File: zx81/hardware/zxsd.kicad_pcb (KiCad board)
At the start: 2 copper layers, 69.9 x 95.9 mm, 40 parts, among them J1 Micro_SD_Card, J2 ZX81_EXP, Q1 BC547, SW1 RESET, U1 74LS32, U10 27C256, U11 KM62256CLP, U2 74HC74, U3 74LS00, U4 74LS02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

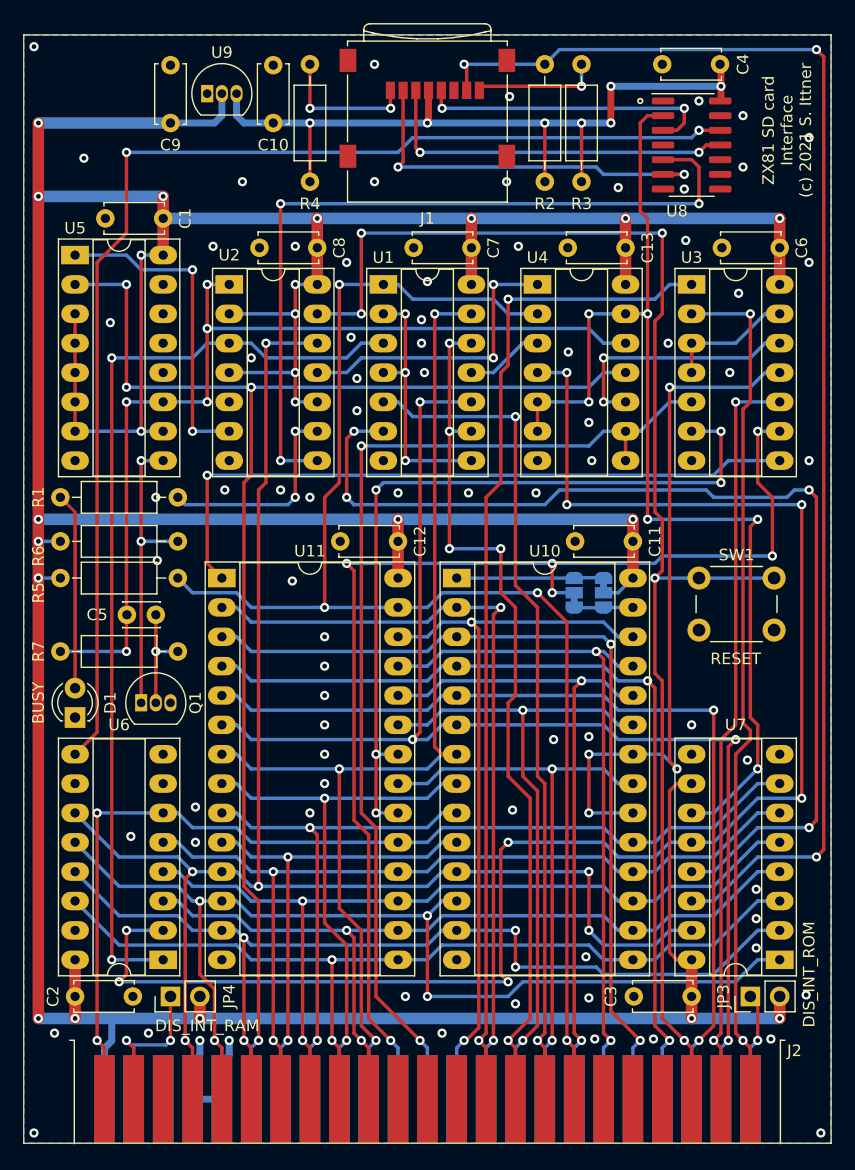
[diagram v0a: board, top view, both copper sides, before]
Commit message: fixed rom chip select
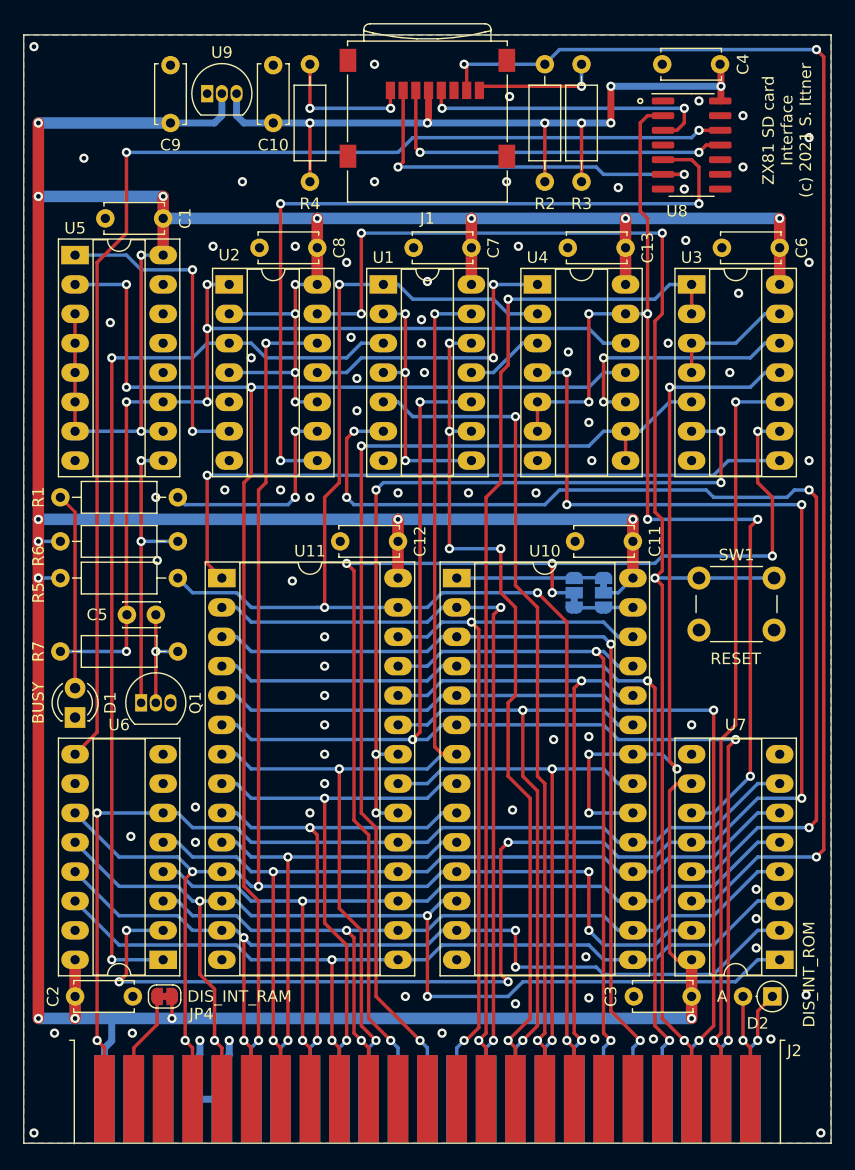
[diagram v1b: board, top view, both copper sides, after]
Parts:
- removed JP3: DIS_INT_ROM, Connector_PinHeader_2.54mm:PinHeader_1x02_P2.54mm_Vertical
- added D2: BAT43, Diode_THT:D_DO-35_SOD27_P2.54mm_Vertical_AnodeUp, F.Cu at (177.2, 126.4)
- C5: value 4p7 -> 470p
- JP4: footprint Connector_PinHeader_2.54mm:PinHeader_1x02_P2.54mm_Vertical -> Jumper:SolderJumper-2_P1.3mm_Bridged_RoundedPad1.0x1.5mm
- U1: value 74LS32 -> 74HCT32
- U2: value 74HC74 -> 74HCT74
- U3: value 74LS00 -> 74HCT00
- U4: value 74LS02 -> 74HCT02
- U5: value 74LS163 -> 74HCT163
- U6: value 74HC165 -> 74HCT165
- U7: value 74HC595 -> 74HCT595
- moved JP4 0.51 mm to (124.6, 126.4), turned to 180 degrees
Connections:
- JP4 pad 1: /nRAMCS_INT -> +5V
- JP4 pad 2: +5V -> /nRAMCS_INT
- U3 pad 2: /nRFSH -> /nMREQ
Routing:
- net /nRFSH: track 74.6 -> 9.15 mm, vias 2 -> 1
- net +5V: track 420.0 -> 410.5 mm, vias 23 -> 22
- net /nRAMCS_INT: track 13.3 -> 9.73 mm, vias 2 -> 0
- net /nMREQ: track 86.9 -> 89.5 mm
- net /SD_CLK: track 95.4 -> 94.9 mm
- net GND: vias 77 -> 76

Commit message: simplified sd card interface
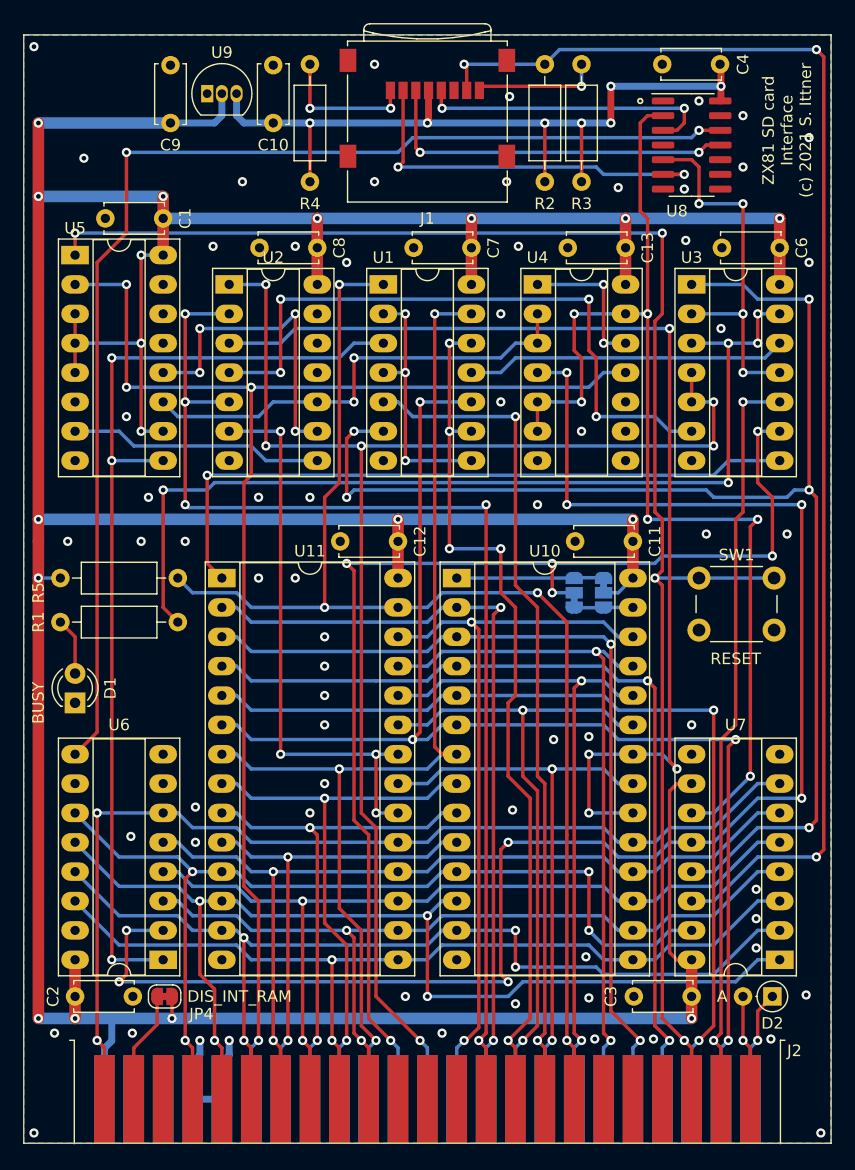
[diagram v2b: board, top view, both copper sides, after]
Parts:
- removed C5: 470p, Capacitor_THT:C_Disc_D3.0mm_W2.0mm_P2.50mm
- removed Q1: BC547, Package_TO_SOT_THT:TO-92_Inline
- removed R6: 1k, Resistor_THT:R_Axial_DIN0207_L6.3mm_D2.5mm_P10.16mm_Horizontal
- removed R7: 47k, Resistor_THT:R_Axial_DIN0207_L6.3mm_D2.5mm_P10.16mm_Horizontal
- U2: value 74HCT74 -> 74HCT32
- moved R1 10.8 mm to (115.6, 94.0)
- moved D1 1.27 mm to (116.8, 101.0)
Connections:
- U2 pad 1: Net-(C5-Pad2) -> /A14
- U2 pad 10: +5V -> Net-(U2-Pad10)
- U2 pad 11: Net-(U2-Pad11) -> (no net)
- U2 pad 12: /D0 -> GND
- U2 pad 13: /nRESET -> GND
- U2 pad 2: +5V -> /nMREQ
- U2 pad 3: /nSDWR -> /nCS_ROM
- U2 pad 4: +5V -> Net-(U2-Pad4)
- U2 pad 5: (no net) -> /nMREQ
- U2 pad 6: Net-(U2-Pad6) -> /nCS_RAM
- U2 pad 8: /nSD_SEL -> Net-(U2-Pad8)
- U2 pad 9: Net-(R1-Pad2) -> Net-(U2-Pad9)
- U3 pad 1: /nMREQ -> /nSDRD
- U3 pad 11: /nCS_ROM -> /nSD_SEL
- U3 pad 12: Net-(U3-Pad12) -> Net-(U1-Pad11)
- U3 pad 13: Net-(U3-Pad13) -> Net-(R1-Pad2)
- U3 pad 2: /nMREQ -> /nSD_SEL
- U3 pad 3: Net-(U3-Pad13) -> Net-(R1-Pad2)
- U3 pad 4: Net-(U3-Pad13) -> /A14
- U3 pad 6: /nCS_RAM -> Net-(U2-Pad4)
- U4 pad 1: Net-(U2-Pad11) -> Net-(U4-Pad1)
- U4 pad 10: Net-(U3-Pad12) -> (no net)
- U4 pad 12: Net-(C5-Pad2) -> Net-(U4-Pad1)
- U4 pad 2: /nWR -> Net-(U2-Pad10)
- U4 pad 3: Net-(U1-Pad11) -> Net-(U2-Pad10)
- U4 pad 8: /A14 -> GND
- U4 pad 9: /A14 -> GND
- U5 pad 1: Net-(U2-Pad6) -> /nRESET
- U5 pad 11: Net-(C5-Pad2) -> Net-(U2-Pad10)
- U5 pad 12: (no net) -> Net-(U2-Pad9)
- U5 pad 6: +5V -> GND
- U5 pad 7: +5V -> Net-(U2-Pad8)
- U5 pad 9: Net-(Q1-Pad1) -> /nSDWR
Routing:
- net Net-(C5-Pad2): track 83.1 -> 0.00 mm, vias 5 -> 0
- net Net-(R1-Pad2): track 18.3 -> 83.3 mm, vias 2 -> 5
- net Net-(U2-Pad4): track 0.00 -> 56.7 mm, vias 0 -> 4
- net /D0: track 134.5 -> 82.8 mm, vias 6 -> 4
- net Net-(U2-Pad10): track 0.00 -> 40.3 mm, vias 0 -> 2
- net /nSD_SEL: track 68.1 -> 32.6 mm, vias 3 -> 4
- net /nCS_ROM: track 60.4 -> 94.0 mm
- net +5V: track 410.5 -> 378.1 mm, vias 22 -> 18
- net /A14: track 91.6 -> 123.0 mm, vias 2 -> 6
- net Net-(U2-Pad6): track 27.8 -> 0.00 mm, vias 2 -> 0
- net Net-(U2-Pad9): track 0.00 -> 27.8 mm, vias 0 -> 4
- net /nSDRD: track 91.3 -> 118.0 mm, vias 4 -> 5
- net Net-(U2-Pad11): track 25.9 -> 0.00 mm, vias 2 -> 0
- net Net-(Q1-Pad1): track 25.4 -> 0.00 mm, vias 2 -> 0
- net Net-(U2-Pad8): track 0.00 -> 22.0 mm
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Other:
- board text removed: "DIS_INT_ROM"

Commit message: cosmetic pcb fixes
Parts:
- moved D1 5.75 mm to (122.6, 100.3)
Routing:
- net Net-(D1-Pad2): track 4.97 -> 10.8 mm, vias 0 -> 1
- net /nSDRD: track 118.0 -> 115.4 mm, vias 5 -> 4
- net /nRESET: track 140.0 -> 138.9 mm
- net /nCS_ROM: track 94.0 -> 94.6 mm
- net GND: vias 66 -> 71

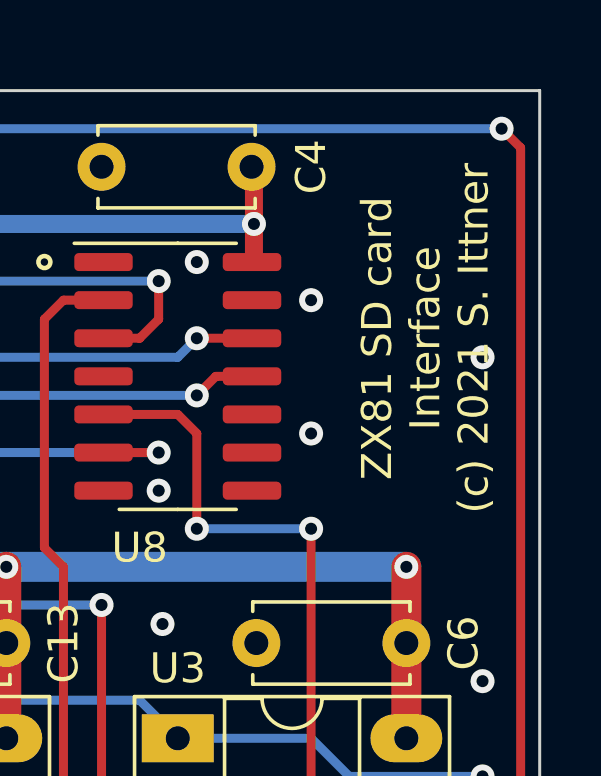
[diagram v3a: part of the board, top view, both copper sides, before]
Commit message: fixed pcb version
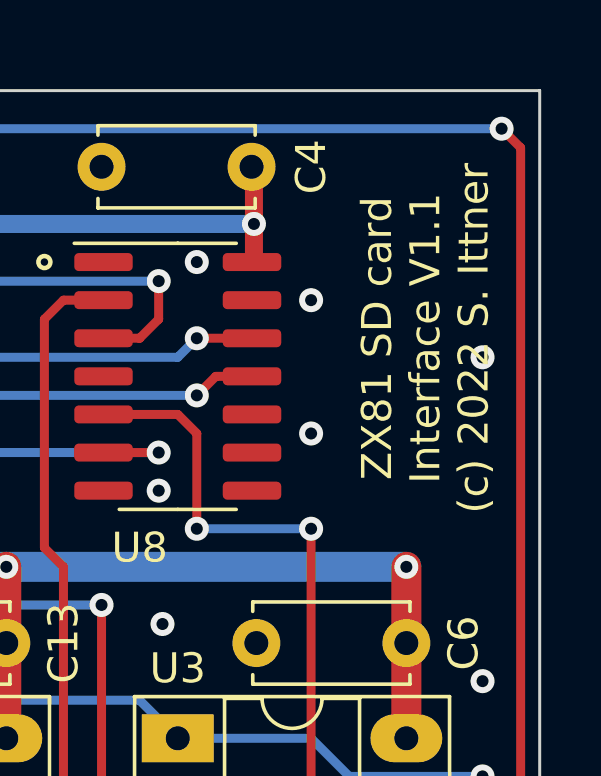
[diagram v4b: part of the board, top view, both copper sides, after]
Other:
- board text added: "ZX81 SD card Interface V1.1 (c) 2022 S. Ittner"
- board text removed: "ZX81 SD card Interface (c) 2021 S. Ittner"
